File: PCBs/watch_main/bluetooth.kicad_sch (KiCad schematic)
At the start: 1 part, among them IC301 nRF52840-QFAA-F-R7

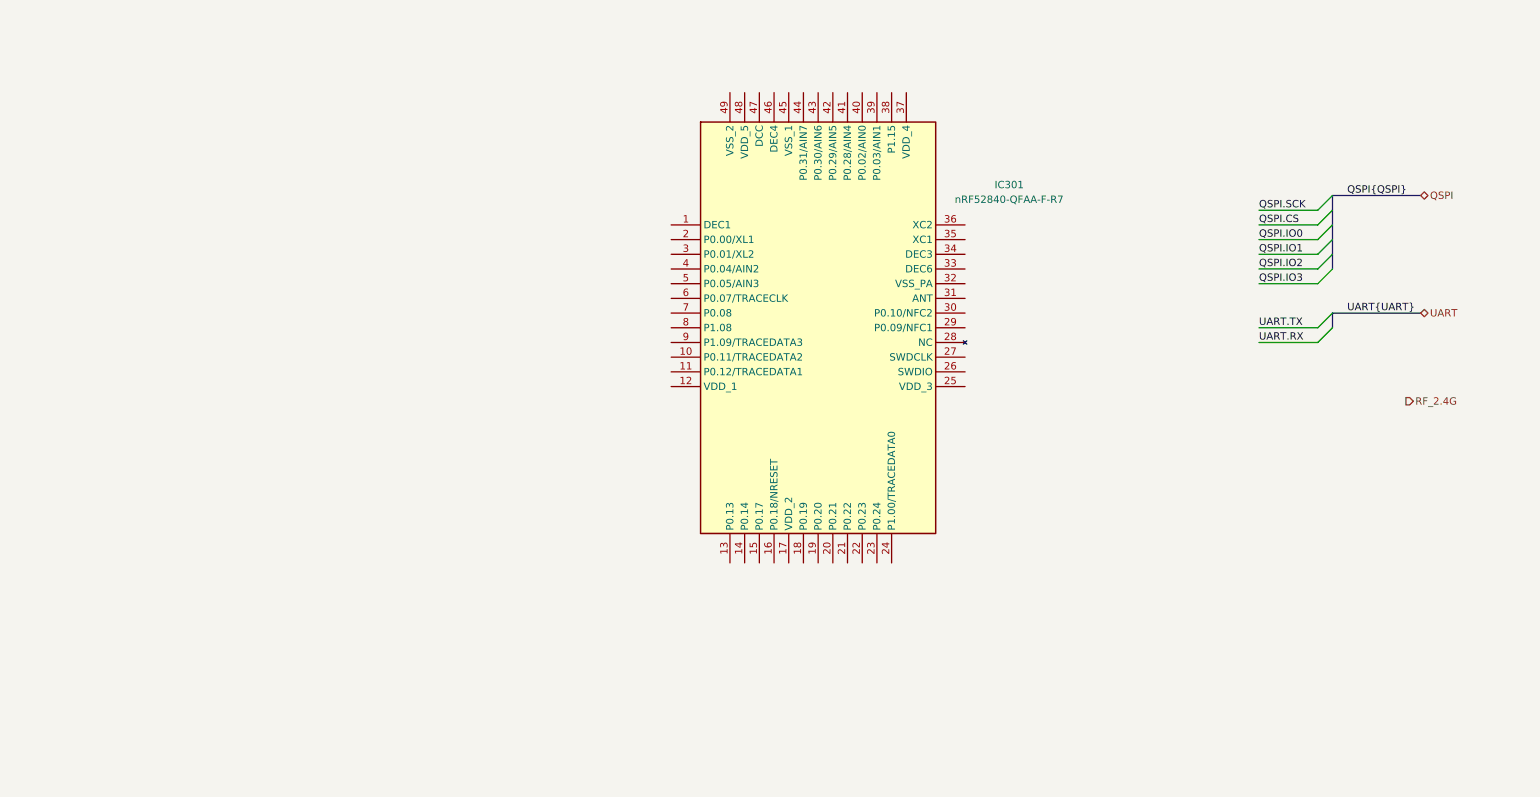
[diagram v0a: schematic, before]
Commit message: Created firmware project
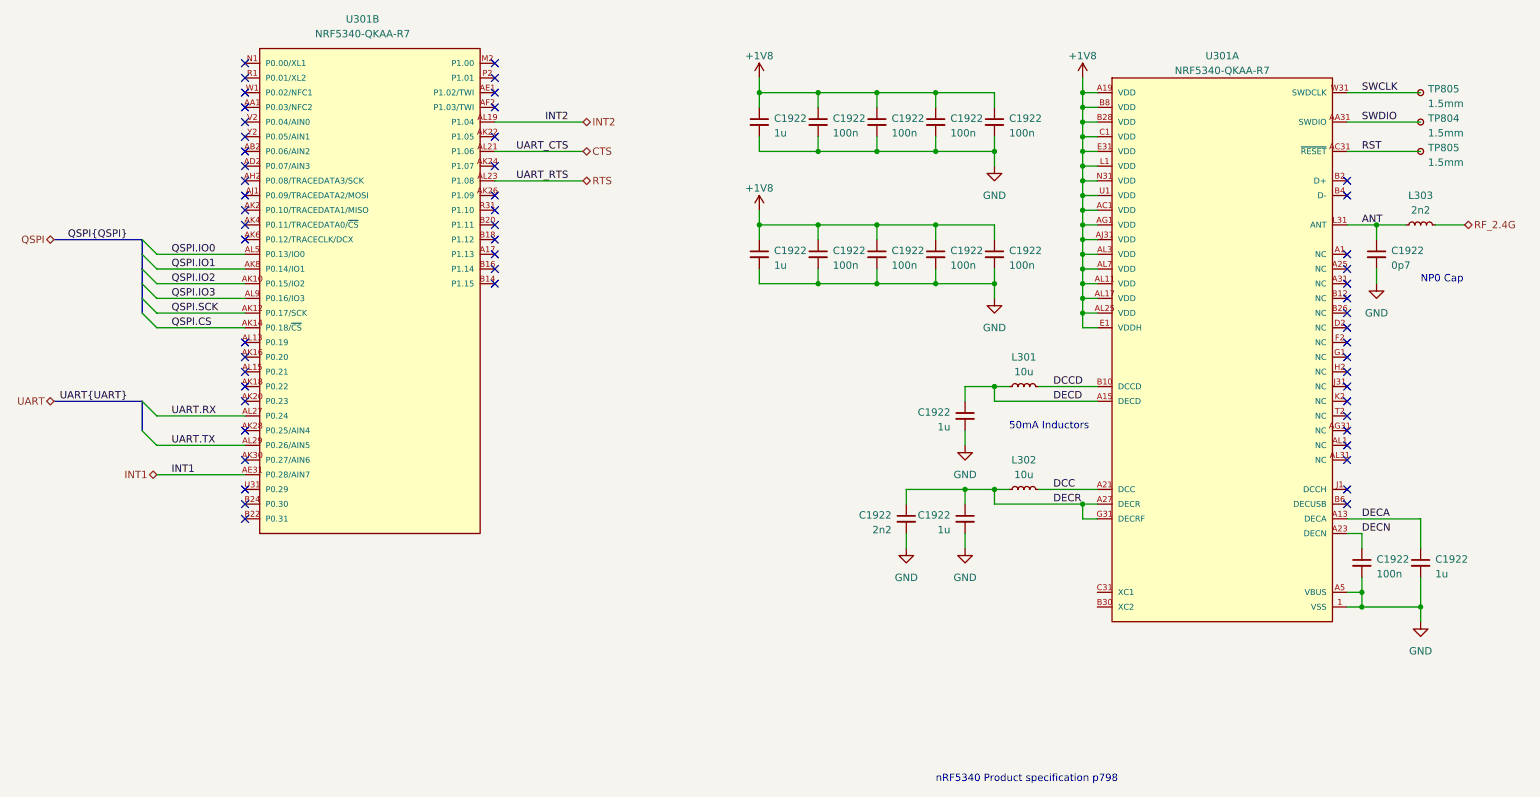
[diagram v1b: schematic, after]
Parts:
- removed IC301: nRF52840-QFAA-F-R7, watch_footprints:QFN40P600X600X95-49N-D, symbol nRF52840-QFAA-F-R7:nRF52840-QFAA-F-R7
- added C1922: 0p7, Capacitor_SMD:C_0402_1005Metric, symbol Device:C_Small
- added C1922: 2n2, Capacitor_SMD:C_0402_1005Metric, symbol Device:C_Small
- added C1922 (x9): 100n, Capacitor_SMD:C_0402_1005Metric, symbol Device:C_Small
- added C1922 (x5): 1u, Capacitor_SMD:C_0402_1005Metric, symbol Device:C_Small
- added L301, L302: 10u, Inductor_SMD:L_0603_1608Metric, symbol Device:L_Small
- added L303: 2n2, Inductor_SMD:L_0402_1005Metric, symbol Device:L_Small
- added TP804, TP805 (x2): 1.5mm, TestPoint:TestPoint_Pad_D1.5mm, symbol Connector:TestPoint_Small
- added U301: NRF5340-QKAA-R7, watch_footprints:NRF5340-QKAA-R7, symbol NRF5340-QKAA-R7:NRF5340-QKAA-R7
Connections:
- net QSPI.CS: now also U301.AK14 (P0.18/~{CS})
- net QSPI.IO0: now also U301.AL5 (P0.13/IO0)
- net QSPI.IO1: now also U301.AK8 (P0.14/IO1)
- net QSPI.IO2: now also U301.AK10 (P0.15/IO2)
- net QSPI.IO3: now also U301.AL9 (P0.16/IO3)
- net QSPI.SCK: now also U301.AK12 (P0.17/SCK)
- net RF_2.4G: now also L303.2
- net UART.RX: now also U301.AL27 (P0.24)
- net UART.TX: now also U301.AL29 (P0.26/AIN5)
- new net +1V8: C1922.1, C1922.1, C1922.1, C1922.1, C1922.1, C1922.1, C1922.1, C1922.1, C1922.1, C1922.1, U301.A19 (VDD), U301.AC1 (VDD), U301.AG1 (VDD), U301.AJ31 (VDD), U301.AL11 (VDD), U301.AL17 (VDD), U301.AL25 (VDD), U301.AL3 (VDD), U301.AL7 (VDD), U301.B28 (VDD), U301.B8 (VDD), U301.C1 (VDD), U301.E1 (VDDH), U301.E31 (VDD), U301.L1 (VDD), U301.N31 (VDD), U301.U1 (VDD)
- new net ANT: C1922.1, L303.1, U301.L31 (ANT)
- new net CTS: U301.AL21 (P1.06)
- new net DCC: L302.2, U301.A21 (DCC)
- new net DCCD: L301.2, U301.B10 (DCCD)
- new net DECA: C1922.1, U301.A13 (DECA)
- new net DECD: C1922.1, L301.1, U301.A15 (DECD)
- new net DECN: C1922.1, U301.A23 (DECN)
- new net DECR: C1922.1, C1922.1, L302.1, U301.A27 (DECR), U301.G31 (DECRF)
- new net GND: C1922.2, C1922.2, C1922.2, C1922.2, C1922.2, C1922.2, C1922.2, C1922.2, C1922.2, C1922.2, C1922.2, C1922.2, C1922.2, C1922.2, C1922.2, C1922.2, U301.1 (VSS), U301.A5 (VBUS)
- new net INT1: U301.AE31 (P0.28/AIN7)
- new net INT2: U301.AL19 (P1.04)
- new net RST: TP805.1, U301.AC31 (~{RESET})
- new net RTS: U301.AL23 (P1.08)
- new net SWCLK: TP805.1, U301.W31 (SWDCLK)
- new net SWDIO: TP804.1, U301.AA31 (SWDIO)
- no-connect marks 0 -> 55
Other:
- note added: "50mA Inductors"
- note added: "NP0 Cap"
- note added: "nRF5340 Product specification p798"

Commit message: Schematic and pcb progress
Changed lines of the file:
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@@
     )
+  )
+  (hierarchical_label "INT2" (shape bidirectional) (at 40.64 121.92 0) (fields_autoplaced)
+    (effects (font (size 1.27 1.27)) (justify left))
   )
   (symbol (lib_id "Device:C_Small") (at 256.54 78.74 0) (unit 1)

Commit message: PCB Schematic progress
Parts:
- added Y301: 32MHz, Crystal:Crystal_SMD_2016-4Pin_2.0x1.6mm, symbol Device:Crystal_GND24_Small
- U301: footprint watch_footprints:NRF5340-QKAA-R7 -> watch_footprints:NRF5340-QKAA-R7_modified
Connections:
- net GND: now also Y301.2, Y301.4
- net XC2: now reaches U301.B30 (XC2)
- net XC2: now also Y301.1
- net XC1: now reaches U301.C31 (XC1)
- net XC1: now also Y301.3
- net INT3: now reaches U301.N1 (P0.00/XL1)
- no-connect marks 55 -> 54
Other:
- moved on the sheet: C1922, L301, L302, L303, TP804, TP805, U301A, U301B

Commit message: Started routing main PCB
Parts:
- L301, L302: footprint Inductor_SMD:L_0603_1608Metric -> Inductor_SMD:L_TDK_MLZ1608
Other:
- title: (none) -> Watch Bluetooth

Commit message: Test rig board finished
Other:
- moved on the sheet: C1922, L301, L302, L303, TP804, TP805, U301A, U301B, Y301
